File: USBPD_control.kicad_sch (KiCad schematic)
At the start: 12 parts, among them SW1 CAS-120TA, U6 TPS65987DDHRSHR

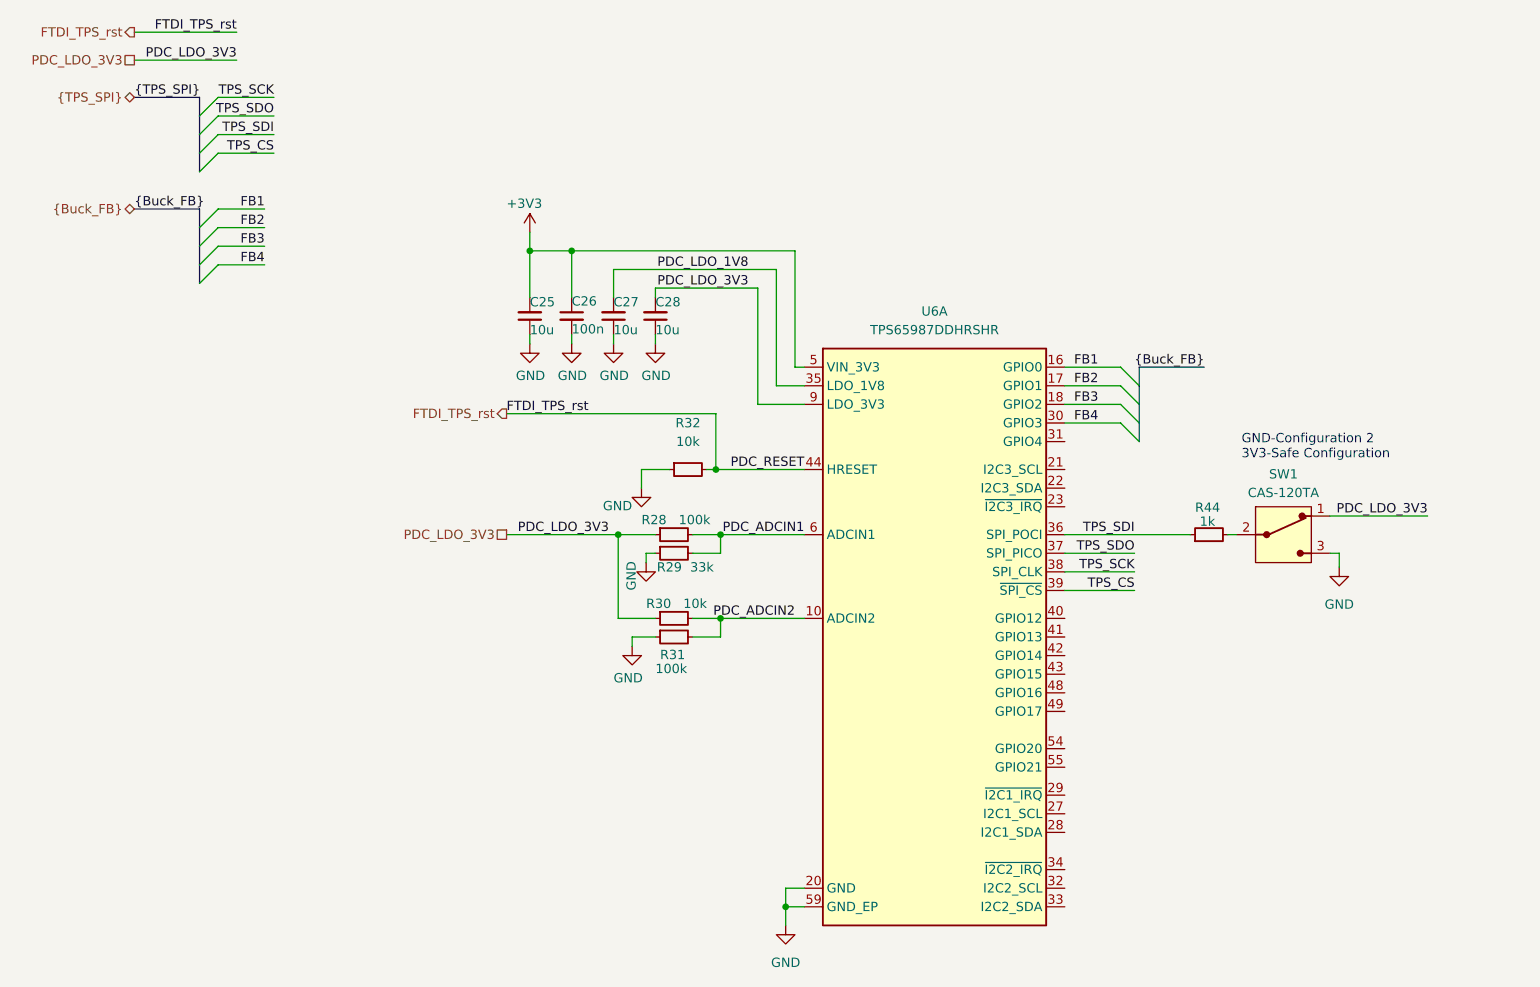
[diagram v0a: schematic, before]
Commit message: [#62623] Improve schematic, change 3V3 buck inductor, correct SPI, add testpoint
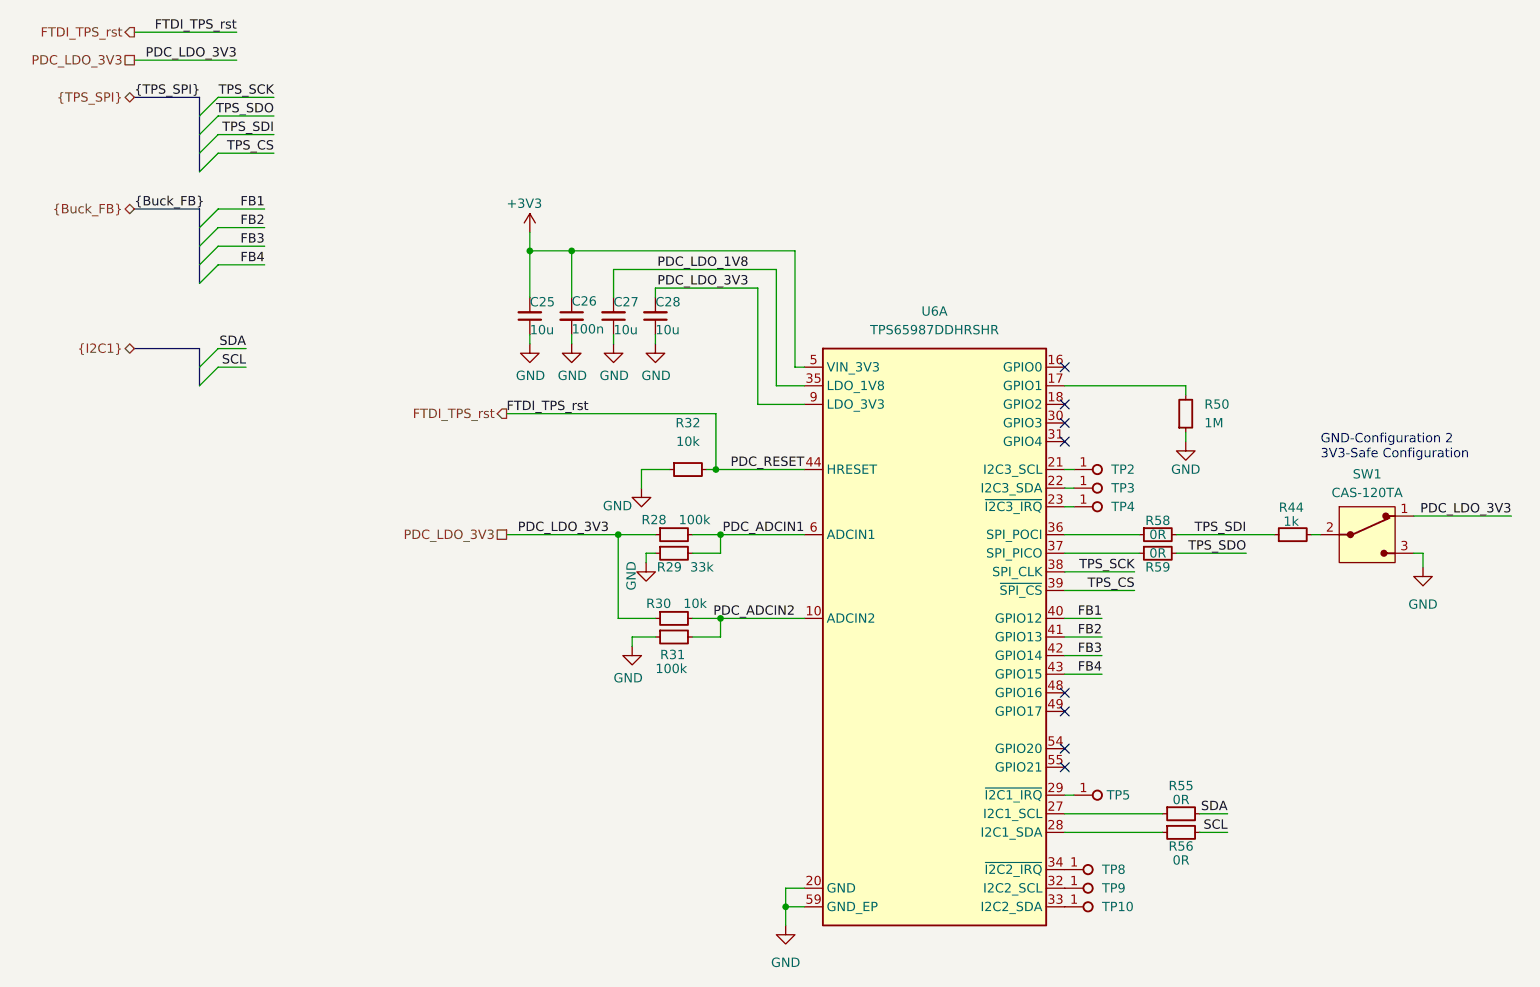
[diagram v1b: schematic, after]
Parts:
- added R50: R_1M_0402, antmicro-footprints:R_0402_1005Metric, symbol antmicroResistors0402:R_1M_0402
- added R55, R56, R58, R59: R_0R_0402, antmicro-footprints:R_0402_1005Metric, symbol antmicroResistors0402:R_0R_0402
- added TP10, TP2, TP3, TP4, TP5, TP8, TP9: TP_0.75mm_SMD, antmicro-footprints:TP_SMD_0.75mm, symbol antmicroTestPoints:TP_0.75mm_SMD
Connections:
- net FB1: now also U6.40 (GPIO12); no longer U6.16 (GPIO0)
- net FB2: now also U6.41 (GPIO13); no longer U6.17 (GPIO1)
- net FB3: now also U6.42 (GPIO14); no longer U6.18 (GPIO2)
- net FB4: now also U6.43 (GPIO15); no longer U6.30 (GPIO3)
- net GND: now also R50.1
- net TPS_SDI: now also R58.2; no longer U6.36 (SPI_POCI)
- net TPS_SDO: now also R59.2; no longer U6.37 (SPI_PICO)
- net at U6.21 (I2C3_SCL): now also TP2.1
- net at U6.22 (I2C3_SDA): now also TP3.1
- net at U6.23 (~{I2C3_IRQ}): now also TP4.1
- net at U6.27 (I2C1_SCL): now also R55.1
- net at U6.28 (I2C1_SDA): now also R56.1
- net at U6.29 (~{I2C1_IRQ}): now also TP5.1
- net at U6.32 (I2C2_SCL): now also TP9.1
- net at U6.33 (I2C2_SDA): now also TP10.1
- net at U6.34 (~{I2C2_IRQ}): now also TP8.1
- new net: R59.1, U6.37 (SPI_PICO)
- new net: R58.1, U6.36 (SPI_POCI)
- new net: R50.2, U6.17 (GPIO1)
- new net SCL: R56.2
- new net SDA: R55.2
- no-connect marks 0 -> 8
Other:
- moved on the sheet: R44, SW1

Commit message: [#62623] Change hierarchy implementation
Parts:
- removed C25, C27, C28: C_10u_0402, antmicro-footprints:C_0402_1005Metric, symbol antmicroCapacitors0402:C_10u_0402
- removed C26: C_100n_0402, antmicro-footprints:C_0402_1005Metric, symbol antmicroCapacitors0402:C_100n_0402
- removed R28, R31: R_100k_0402, antmicro-footprints:R_0402_1005Metric, symbol antmicroResistors0402:R_100k_0402
- removed R29: R_33k_0402, antmicro-footprints:R_0402_1005Metric, symbol antmicroResistors0402:R_33k_0402
- removed R30, R32: R_10k_0402, antmicro-footprints:R_0402_1005Metric, symbol antmicroResistors0402:R_10k_0402
- removed R44: R_1k_0402, antmicro-footprints:R_0402_1005Metric, symbol antmicroResistors0402:R_1k_0402
- removed R50: R_1M_0402, antmicro-footprints:R_0402_1005Metric, symbol antmicroResistors0402:R_1M_0402
- removed R55, R56, R58, R59: R_0R_0402, antmicro-footprints:R_0402_1005Metric, symbol antmicroResistors0402:R_0R_0402
- removed SW1: CAS-120TA, antmicro-footprints:Switch_Slide_CAS-120TA, symbol antmicroSlideSwitches:CAS-120TA
- removed TP10, TP2, TP3, TP4, TP5, TP8, TP9: TP_0.75mm_SMD, antmicro-footprints:TP_SMD_0.75mm, symbol antmicroTestPoints:TP_0.75mm_SMD
- removed U6: TPS65987DDHRSHR, antmicro-footprints:IC_TPS65987DDHRSHR, symbol antmicroInterfaceControllers:TPS65987DDHRSHR
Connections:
- no-connect marks 8 -> 0
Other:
- note removed: "GND-Configuration 2 3V3-Safe Configuration"
